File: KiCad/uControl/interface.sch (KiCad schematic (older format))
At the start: 66 parts, among them M1 MANIFOLD, P10 C3SB, P11 VSel_Vlv, P12 Valve_Conn, P13 Valve_Conn_BO, P14 Valve, P15 Flow_Conn, P16 FlowMeter, P17 Pump_Conn, P18 Pump_Conn_BO, P19 Pump_Conn_Flex, P20 Temp_Conn, P21 Temp_Conn_BO, P22 Temp, P23 Pump, P6 Pulse, P7 Gage_Pr, P8 Abso_Pr, P9 C3SB, Q1 2SD1834T100, U1 TXB0104D, U2 TXS0102DCT

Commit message: uControl Board layout work in progress
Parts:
- P20, P21: footprint Header_2x2 -> SIL-4
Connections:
- net MISO: no longer P7.4 (P4), U1.2 (A1)
- net SCK: no longer P7.5 (P5), U1.3 (A2)
- net ~MOSI: no longer P7.8 (P8), U1.5 (A4)
- net ~SS: no longer P7.6 (P6), U1.4 (A3)
- net +Vlv: now reaches C13.1, D1.2 (K), P11.2 (P2), P12.1 (P1)
- net TD: now reaches P21.4 (P4), P22.1
- net T-: now reaches C16.1, P21.3 (P3), P22.2
- net T+: now reaches C16.2, P21.2 (P2), P22.5
- net TC: now reaches P21.1 (P1), P22.6
- net TSCL: now reaches P20.4 (P4), U2.4 (A2)
- net TSDA: now reaches P20.1 (P1), U2.5 (A1)
- net P+: now reaches P18.1, P19.1
- net P+: now also P18.2, P19.2
- net P-: now reaches P18.3, P19.3
- net PX: now reaches P18.4, P19.4
- net PR: now reaches P18.5, P19.5
- net PT: now reaches P18.6, P19.6
- new net P_MISO: P7.4 (P4), U1.2 (A1)
- new net P_MOSI: P7.8 (P8), U1.5 (A4)
- new net P_SCK: P7.5 (P5), U1.3 (A2)
- new net P_SS: P7.6 (P6), U1.4 (A3)
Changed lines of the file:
@@
-EESchema Schematic File Version 2  date 12/27/2012 6:53:46 PM
+EESchema Schematic File Version 2  date Thursday 27 December 2012 10:04:40 PM IST
 LIBS:uControl
 LIBS:Conn-raspberry
@@
 Comment4 ""
 $EndDescr
+Text Label 6750 3600 0    40   ~ 0
++Vlv
+Text Label 7700 6375 0    40   ~ 0
+TC
+Text Label 7700 6275 0    40   ~ 0
+T+
+Text Label 7700 5975 0    40   ~ 0
+T-
+Text Label 7700 5875 0    40   ~ 0
+TD
+Text Label 6325 6275 0    40   ~ 0
+TSCL
+Text Label 6325 6175 0    40   ~ 0
+TSDA
+Text Label 4275 5850 0    40   ~ 0
+PT
+Text Label 4275 5750 0    40   ~ 0
+PR
+Text Label 4275 5650 0    40   ~ 0
+PX
+Text Label 4275 5550 0    40   ~ 0
+P-
+Text Label 4275 5450 0    40   ~ 0
+P+
+Text Label 4275 5350 0    40   ~ 0
+P+
+Text Label 2925 3425 0    40   ~ 0
+PD2_Flow_Tx
 $Comp
 L SCREW SC21
@@
 F 0 "P21" V 7200 6125 50  0000 C CNN
 F 1 "Temp_Conn_BO" V 7300 6125 40  0000 C CNN
-F 2 "Header_2x2" V 7400 6125 40  0001 C CNN
+F 2 "SIL-4" V 7400 6125 40  0001 C CNN
 	1    7250 6125
 	-1   0    0    1
@@
 F 0 "P20" V 6975 6125 50  0000 C CNN
 F 1 "Temp_Conn" V 7075 6125 40  0000 C CNN
-F 2 "Header_2x2" V 7175 6125 40  0001 C CNN
+F 2 "SIL-4" V 7175 6125 40  0001 C CNN
 	1    7025 6125
 	1    0    0    -1
@@
 $EndComp
 Text Label 2950 1175 0    40   ~ 0
-SCK
+P_SCK
 NoConn ~ 3325 1375
 Text Label 2950 1475 0    40   ~ 0
-~MOSI
+P_MOSI
 Text Label 2950 1275 0    40   ~ 0
-~SS
+P_SS
 Text Label 2950 1075 0    40   ~ 0
-MISO
+P_MISO
 Text Label 2950 975  0    40   ~ 0
 PC3_Pr1

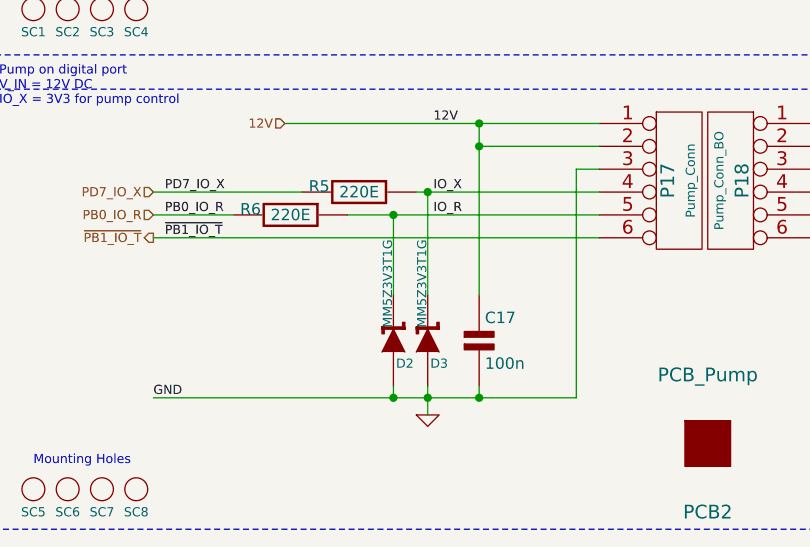
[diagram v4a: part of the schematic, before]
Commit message: uControl changed to Thru Hole design. Basic parts laid out. No tracks yet.
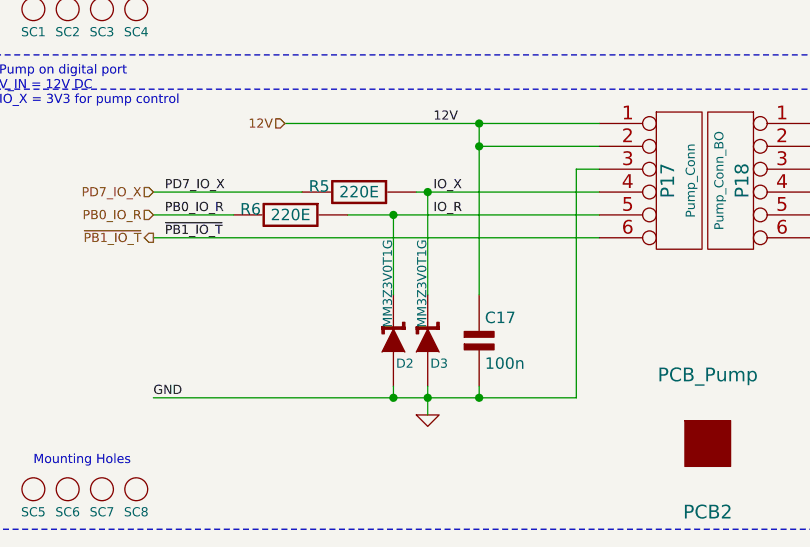
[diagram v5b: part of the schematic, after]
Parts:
- C10, C11, C12, C13, C14, C15, C17, C5, C6, C7, C8, C9: footprint c_0805 -> C2
- D1: footprint S1A-E3 -> diode_do41
- D2, D3: value MM5Z3V3T1G -> MM3Z3V0T1G; footprint MM5Z3V3T1G -> diode_do35
- P10, P9: footprint SIL-4 -> pin_strip_4-90
- P6: footprint SIL-3 -> pin_strip_3-90
- Q1: footprint 2SD1834 -> TO220-3-V
- R4, R5, R6, R7: footprint r_0805 -> rc03_vert
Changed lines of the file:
@@
-EESchema Schematic File Version 2  date Thursday 27 December 2012 10:04:40 PM IST
+EESchema Schematic File Version 2  date 12/28/2012 6:29:01 PM
 LIBS:uControl
 LIBS:Conn-raspberry
@@
 Sheet 2 5
 Title ""
-Date "27 dec 2012"
+Date "28 dec 2012"
 Rev ""
 Comp ""
@@
 F 0 "P10" V 10375 2600 50  0000 C CNN
 F 1 "C3SB" V 10475 2600 50  0000 C CNN
-F 2 "SIL-4" V 10575 2600 50  0001 C CNN
+F 2 "pin_strip_4-90" V 10575 2600 50  0001 C CNN
 	1    10425 2600
 	1    0    0    -1
@@
 F 0 "C11" H 10800 2650 50  0000 L CNN
 F 1 "100n" H 10800 2475 50  0000 L CNN
-F 2 "c_0805" H 10800 2575 50  0001 C CNN
+F 2 "C2" H 10800 2575 50  0001 C CNN
 F 4 "490-1734-1-ND" H 10775 2775 60  0001 C CNN "Digikey"
 	1    10775 2575
@@
 F 0 "C9" H 10800 1800 50  0000 L CNN
 F 1 "100n" H 10800 1625 50  0000 L CNN
-F 2 "c_0805" H 10800 1725 50  0001 C CNN
+F 2 "C2" H 10800 1725 50  0001 C CNN
 F 4 "490-1734-1-ND" H 10775 1925 60  0001 C CNN "Digikey"
 	1    10775 1725
@@
 F 0 "P9" V 10375 1750 50  0000 C CNN
 F 1 "C3SB" V 10475 1750 50  0000 C CNN
-F 2 "SIL-4" V 10575 1750 50  0001 C CNN
+F 2 "pin_strip_4-90" V 10575 1750 50  0001 C CNN
 	1    10425 1750
 	1    0    0    -1
@@
 $EndComp
 $Comp
-L GND #PWR03
+L GND #PWR8
 U 1 1 50CCC2AC
 P 6425 5975
-F 0 "#PWR03" H 6425 5975 30  0001 C CNN
+F 0 "#PWR8" H 6425 5975 30  0001 C CNN
 F 1 "GND" H 6425 5905 30  0001 C CNN
 	1    6425 5975
@@
 F 0 "C15" H 6450 5775 50  0000 L CNN
 F 1 "100n" H 6450 5625 50  0000 L CNN
-F 2 "c_0805" H 6450 5725 50  0001 C CNN
+F 2 "C2" H 6450 5725 50  0001 C CNN
 F 4 "490-1734-1-ND" H 6425 5900 60  0001 C CNN "Digikey"
 	1    6425 5700
@@
 F 0 "C14" H 5275 5775 50  0000 L CNN
 F 1 "100n" H 5275 5625 50  0000 L CNN
-F 2 "c_0805" H 5275 5725 50  0001 C CNN
+F 2 "C2" H 5275 5725 50  0001 C CNN
 F 4 "490-1734-1-ND" H 5250 5900 60  0001 C CNN "Digikey"
 	1    5250 5700
@@
 $EndComp
 $Comp
-L GND #PWR04
+L GND #PWR6
 U 1 1 50CCC292
 P 5250 5950
-F 0 "#PWR04" H 5250 5950 30  0001 C CNN
+F 0 "#PWR6" H 5250 5950 30  0001 C CNN
 F 1 "GND" H 5250 5880 30  0001 C CNN
 	1    5250 5950
@@
 F 0 "R7" H 6225 6475 50  0000 C CNN
 F 1 "10k" V 6275 6625 50  0000 C CNN
-F 2 "r_0805" V 6375 6625 50  0001 C CNN
+F 2 "rc03_vert" V 6375 6625 50  0001 C CNN
 	1    6275 6625
 	-1   0    0    1
@@
 5V0
 $Comp
-L GND #PWR05
+L GND #PWR7
 U 1 1 50CCC1EF
 P 5800 7000
-F 0 "#PWR05" H 5800 7000 30  0001 C CNN
+F 0 "#PWR7" H 5800 7000 30  0001 C CNN
 F 1 "GND" H 5800 6930 30  0001 C CNN
 	1    5800 7000
@@
 F 0 "R4" H 2375 2375 50  0000 C CNN
 F 1 "10k" V 2425 2550 50  0000 C CNN
-F 2 "r_0805" V 2525 2550 50  0001 C CNN
+F 2 "rc03_vert" V 2525 2550 50  0001 C CNN
 	1    2425 2550
 	-1   0    0    1
@@
 $EndComp
 $Comp
-L GND #PWR06
+L GND #PWR4
 U 1 1 50CCABF0
 P 2575 1650
-F 0 "#PWR06" H 2575 1650 30  0001 C CNN
+F 0 "#PWR4" H 2575 1650 30  0001 C CNN
 F 1 "GND" H 2575 1580 30  0001 C CNN
 	1    2575 1650
@@
 $EndComp
 $Comp
-L GND #PWR07
+L GND #PWR2
 U 1 1 50CCABEC
 P 1450 1650
-F 0 "#PWR07" H 1450 1650 30  0001 C CNN
+F 0 "#PWR2" H 1450 1650 30  0001 C CNN
 F 1 "GND" H 1450 1580 30  0001 C CNN
 	1    1450 1650
@@
 F 0 "C7" H 1475 1475 50  0000 L CNN
 F 1 "100n" H 1475 1325 50  0000 L CNN
-F 2 "c_0805" H 1475 1425 50  0001 C CNN
+F 2 "C2" H 1475 1425 50  0001 C CNN
 F 4 "490-1734-1-ND" H 1450 1600 60  0001 C CNN "Digikey"
 	1    1450 1400
@@
 F 0 "C8" H 2600 1475 50  0000 L CNN
 F 1 "100n" H 2600 1325 50  0000 L CNN
-F 2 "c_0805" H 2600 1425 50  0001 C CNN
+F 2 "C2" H 2600 1425 50  0001 C CNN
 F 4 "490-1734-1-ND" H 2575 1600 60  0001 C CNN "Digikey"
 	1    2575 1400
@@
 $EndComp
 $Comp
-L GND #PWR08
+L GND #PWR3
 U 1 1 50CCAA70
 P 1900 2900
-F 0 "#PWR08" H 1900 2900 30  0001 C CNN
+F 0 "#PWR3" H 1900 2900 30  0001 C CNN
 F 1 "GND" H 1900 2830 30  0001 C CNN
 	1    1900 2900
@@
 F 0 "C5" H 6575 1025 50  0000 L CNN
 F 1 "100n" H 6575 875 50  0000 L CNN
-F 2 "c_0805" H 6575 975 50  0001 C CNN
+F 2 "C2" H 6575 975 50  0001 C CNN
 F 4 "490-1734-1-ND" H 6550 1150 60  0001 C CNN "Digikey"
 	1    6550 950
@@
 F 0 "C13" H 7025 4700 50  0000 L CNN
 F 1 "100n" H 7025 4500 50  0000 L CNN
-F 2 "c_0805" H 7025 4600 50  0001 C CNN
+F 2 "C2" H 7025 4600 50  0001 C CNN
 F 4 "490-1734-1-ND" H 7000 4800 60  0001 C CNN "Digikey"
 	1    7000 4600
@@
 F 0 "C17" H 2825 6400 50  0000 L CNN
 F 1 "100n" H 2825 6200 50  0000 L CNN
-F 2 "c_0805" H 2825 6300 50  0001 C CNN
+F 2 "C2" H 2825 6300 50  0001 C CNN
 F 4 "490-1734-1-ND" H 2800 6500 60  0001 C CNN "Digikey"
 	1    2800 6300
@@
 F 0 "C12" H 3225 4450 50  0000 L CNN
 F 1 "100n" H 3225 4275 50  0000 L CNN
-F 2 "c_0805" H 3225 4375 50  0001 C CNN
+F 2 "C2" H 3225 4375 50  0001 C CNN
 F 4 "490-1734-1-ND" H 3200 4575 60  0001 C CNN "Digikey"
 	1    3200 4375
@@
 F 0 "C10" H 3250 2575 50  0000 L CNN
 F 1 "100n" H 3250 2425 50  0000 L CNN
-F 2 "c_0805" H 3250 2525 50  0001 C CNN
+F 2 "C2" H 3250 2525 50  0001 C CNN
 F 4 "490-1734-1-ND" H 3225 2700 60  0001 C CNN "Digikey"
 	1    3225 2500
@@
 F 0 "C6" H 10800 1075 50  0000 L CNN
 F 1 "100n" H 10800 900 50  0000 L CNN
-F 2 "c_0805" H 10800 1000 50  0001 C CNN
+F 2 "C2" H 10800 1000 50  0001 C CNN
 F 4 "490-1734-1-ND" H 10775 1200 60  0001 C CNN "Digikey"
 	1    10775 1000
@@
 F 0 "P6" V 10375 1000 50  0000 C CNN
 F 1 "Pulse" V 10475 1000 50  0000 C CNN
-F 2 "SIL-3" V 10575 1000 50  0001 C CNN
+F 2 "pin_strip_3-90" V 10575 1000 50  0001 C CNN
 	1    10425 1000
 	1    0    0    -1
@@
 P 2425 6300
 F 0 "D2" V 2325 6250 40  0000 C CNN
-F 1 "MM5Z3V3T1G" H 2675 6325 40  0000 C CNN
-F 2 "MM5Z3V3T1G" H 2675 6350 40  0001 C CNN
+F 1 "MM3Z3V0T1G" H 2675 6325 40  0000 C CNN
+F 2 "diode_do35" H 2675 6350 40  0001 C CNN
 	1    2425 6300
 	0    -1   -1   0
@@
 F 0 "R6" V 1950 5575 50  0000 C CNN
 F 1 "220E" V 1975 5750 50  0000 C CNN
-F 2 "r_0805" V 2075 5750 50  0001 C CNN
+F 2 "rc03_vert" V 2075 5750 50  0001 C CNN
 	1    1975 5750
 	0    1    1    0
@@
 F 0 "D1" V 6325 4000 40  0000 C CNN
 F 1 "S1A-E3/61T" H 6425 3850 40  0000 C CNN
-F 2 "S1A-E3" H 6425 3950 40  0001 C CNN
+F 2 "diode_do41" H 6425 3950 40  0001 C CNN
 	1    6425 3950
 	0    -1   -1   0
@@
 12V
 $Comp
-L GND #PWR09
+L GND #PWR9
 U 1 1 50B4B058
 P 6750 4975
-F 0 "#PWR09" H 6750 4975 30  0001 C CNN
+F 0 "#PWR9" H 6750 4975 30  0001 C CNN
 F 1 "GND" H 6750 4905 30  0001 C CNN
 	1    6750 4975
@@
 $EndComp
 $Comp
-L GND #PWR010
+L GND #PWR5
 U 1 1 50B4B052
 P 2575 6625
-F 0 "#PWR010" H 2575 6625 30  0001 C CNN
+F 0 "#PWR5" H 2575 6625 30  0001 C CNN
 F 1 "GND" H 2575 6555 30  0001 C CNN
 	1    2575 6625
@@
 F 0 "Q1" H 6525 4525 50  0000 C CNN
 F 1 "2SD1834T100" H 6375 4450 50  0000 C CNN
-F 2 "2SD1834" H 6840 4600 30  0001 C CNN
+F 2 "TO220-3-V" H 6840 4600 30  0001 C CNN
 	1    6650 4600
 	1    0    0    -1
@@
 F 0 "R5" V 2250 5475 50  0000 C CNN
 F 1 "220E" V 2275 5650 50  0000 C CNN
-F 2 "r_0805" V 2375 5650 50  0001 C CNN
+F 2 "rc03_vert" V 2375 5650 50  0001 C CNN
 	1    2275 5650
 	0    1    1    0
@@
 P 2575 6300
 F 0 "D3" V 2475 6250 40  0000 C CNN
-F 1 "MM5Z3V3T1G" H 2825 6325 40  0000 C CNN
-F 2 "MM5Z3V3T1G" H 2825 6350 40  0001 C CNN
+F 1 "MM3Z3V0T1G" H 2825 6325 40  0000 C CNN
+F 2 "diode_do35" H 2825 6350 40  0001 C CNN
 	1    2575 6300
 	0    -1   -1   0
